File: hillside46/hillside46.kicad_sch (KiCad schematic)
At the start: 92 parts, among them J1 I2C, J2 TRRS, J3 Bat_Pos, J4 Bat_Neg, J5 FFC2B28-12-G, K1 SW_Key, K10 SW_Key, K11 SW_Key, K12 SW_Key, K13 SW_Key, K14 SW_Key, K15 SW_Key, K16 SW_Key, K17 SW_Key, K18 SW_Key, K19 SW_Rotary, K2 SW_Key, K20 SW_Rotary, K21 SW_Key, K22 SW_Key, K23 SW_Key, K3 SW_Key, K4 SW_Key, K5 SW_Key, K6 SW_Key, K7 SW_Key, K8 SW_Key, K9 SW_Key, SW1 SKQGAFE010, SW2 SW_Power, U1 NiceNano2_r, U2 SRV05-4

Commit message: Adding some JLCPCB part numbers
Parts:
- J5: JLC Type (none) -> Extended; LCSC (none) -> C271734; Price (none) -> 0.4155 @ 2+
- SW2: Config Optional -> (none); LCSC (none) -> C221662
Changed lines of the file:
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@@
       (effects (font (size 1.27 1.27)) hide)
     )
-    (property "LCSC" "" (id 4) (at 55.88 180.34 0)
+    (property "LCSC" "C221662" (id 4) (at 55.88 180.34 0)
       (effects (font (size 1.27 1.27)) hide)
     )
@@
       (effects (font (size 1.27 1.27)) hide)
     )
-    (property "Config" "Optional" (id 7) (at 55.88 180.34 0)
+    (property "Config" "" (id 7) (at 55.88 180.34 0)
       (effects (font (size 1.27 1.27)) hide)
     )
@@
       (effects (font (size 1.27 1.27)) (justify left bottom) hide)
     )
-    (pin "1")
+    (property "JLC Type" "Extended" (id 8) (at 243.84 146.05 0)
+      (effects (font (size 1.27 1.27)) hide)
+    )
+    (property "LCSC" "C271734" (id 9) (at 243.84 146.05 0)
+      (effects (font (size 1.27 1.27)) hide)
+    )
+    (property "Price" "0.4155 @ 2+" (id 10) (at 243.84 146.05 0)
+      (effects (font (size 1.27 1.27)) hide)
+    )
+    (pin "1")

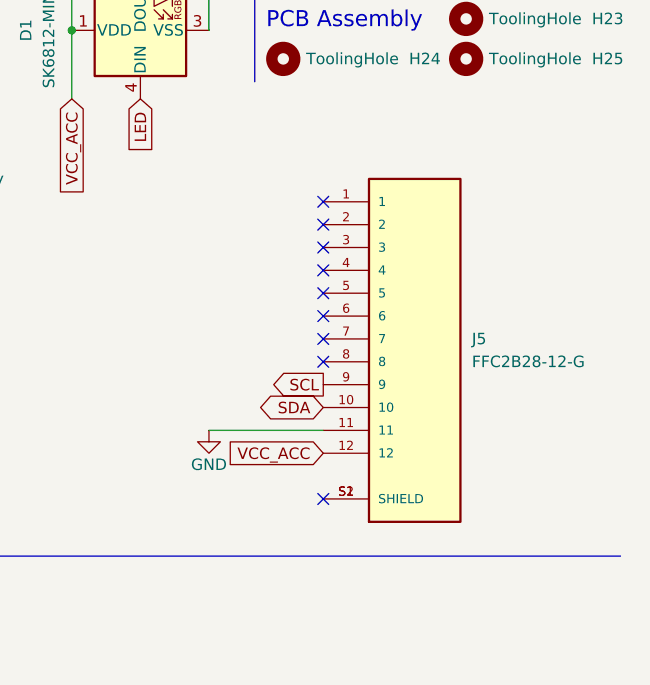
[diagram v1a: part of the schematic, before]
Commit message: Updating FFC connector to use the same footprint as JLCPCB part and rotating by 180 degrees to orient correctly
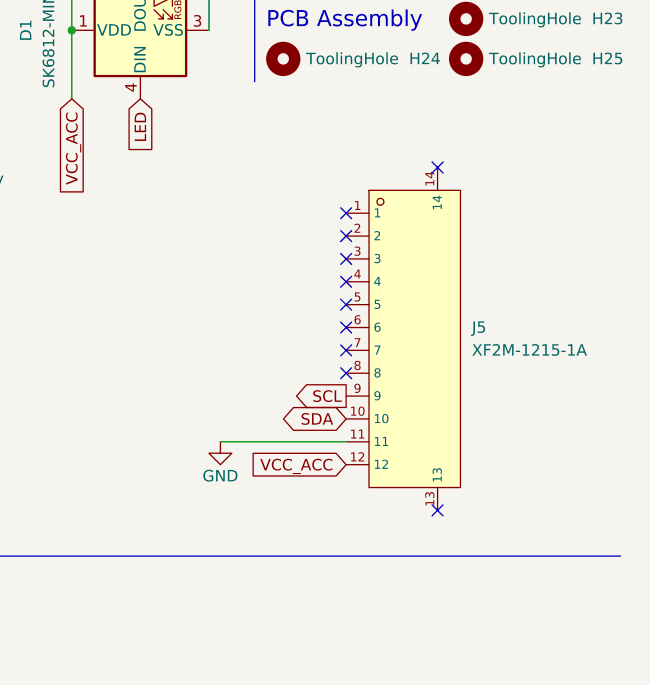
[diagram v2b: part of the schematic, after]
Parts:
- J5: value FFC2B28-12-G -> XF2M-1215-1A; footprint GCT_FFC2B28-12-G -> XF2M-1215-1A:FPC-SMD_12P-P0.50_XF2M-1215-1A; symbol FFC2B28-12-G:FFC2B28-12-G -> XF2M-1215-1A:XF2M-1215-1A
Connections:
- no-connect marks 14 -> 15
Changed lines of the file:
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@@
   (junction (at 176.53 142.24) (diameter 0) (color 0 0 0 0)
   )
-  (no_connect (at 233.68 163.83))
   (no_connect (at 213.36 50.8))
   (no_connect (at 102.87 154.94))
   (no_connect (at 135.255 184.15))
-  (no_connect (at 233.68 148.59))
-  (no_connect (at 233.68 143.51))
-  (no_connect (at 233.68 146.05))
-  (no_connect (at 233.68 138.43))
+  (no_connect (at 246.38 165.1))
+  (no_connect (at 236.22 134.62))
+  (no_connect (at 236.22 137.16))
+  (no_connect (at 236.22 139.7))
+  (no_connect (at 236.22 132.08))
+  (no_connect (at 236.22 149.86))
+  (no_connect (at 236.22 142.24))
+  (no_connect (at 236.22 144.78))
+  (no_connect (at 236.22 147.32))
+  (no_connect (at 246.38 127))
   (no_connect (at 99.06 154.94))
-  (no_connect (at 233.68 140.97))
-  (no_connect (at 233.68 130.81))
-  (no_connect (at 233.68 133.35))
-  (no_connect (at 233.68 135.89))
   (no_connect (at 60.96 177.8))
   (wire (pts (xy 172.72 57.15) (xy 180.975 57.15))
@@
     (stroke (width 0) (type default) (color 0 0 0 0))
   )
-  (wire (pts (xy 220.98 156.21) (xy 233.68 156.21))
-    (stroke (width 0) (type default) (color 0 0 0 0))
-  )
   (wire (pts (xy 14.605 36.195) (xy 14.605 50.165))
     (stroke (width 0) (type default) (color 0 0 0 0))
@@
     (stroke (width 0) (type default) (color 0 0 0 0))
   )
+  (wire (pts (xy 222.25 157.48) (xy 236.22 157.48))
+    (stroke (width 0) (type default) (color 0 0 0 0))
+  )
   (wire (pts (xy 220.98 93.98) (xy 220.98 76.2))
     (stroke (width 0) (type default) (color 0 0 0 0))
@@
     )
   )
-  (global_label "SCL" (shape output) (at 233.68 151.13 180) (fields_autoplaced)
+  (global_label "SCL" (shape output) (at 236.22 152.4 180) (fields_autoplaced)
     (effects (font (size 1.27 1.27)) (justify right))
-    (property "Intersheet References" "${INTERSHEET_REFS}" (id 0) (at 420.37 281.94 0)
+    (property "Intersheet References" "${INTERSHEET_REFS}" (id 0) (at 422.91 283.21 0)
       (effects (font (size 1.27 1.27)) hide)
     )
@@
     )
   )
-  (global_label "VCC_ACC" (shape input) (at 233.68 158.75 180) (fields_autoplaced)
+  (global_label "VCC_ACC" (shape input) (at 236.22 160.02 180) (fields_autoplaced)
     (effects (font (size 1.27 1.27)) (justify right))
-    (property "Intersheet References" "${INTERSHEET_REFS}" (id 0) (at 58.42 27.94 0)
+    (property "Intersheet References" "${INTERSHEET_REFS}" (id 0) (at 60.96 29.21 0)
       (effects (font (size 1.27 1.27)) hide)
     )
@@
     )
   )
-  (global_label "SDA" (shape bidirectional) (at 233.68 153.67 180) (fields_autoplaced)
+  (global_label "SDA" (shape bidirectional) (at 236.22 154.94 180) (fields_autoplaced)
     (effects (font (size 1.27 1.27)) (justify right))
-    (property "Intersheet References" "${INTERSHEET_REFS}" (id 0) (at 420.37 290.83 0)
+    (property "Intersheet References" "${INTERSHEET_REFS}" (id 0) (at 422.91 292.1 0)
       (effects (font (size 1.27 1.27)) hide)
     )
@@
     )
   )
-  (symbol (lib_id "power:GND") (at 220.98 156.21 0) (unit 1)
+  (symbol (lib_id "power:GND") (at 222.25 157.48 0) (unit 1)
     (in_bom yes) (on_board yes)
-    (property "Reference" "#PWR0105" (id 0) (at 220.98 162.56 0)
+    (property "Reference" "#PWR0105" (id 0) (at 222.25 163.83 0)
       (effects (font (size 1.27 1.27)) hide)
     )
-    (property "Value" "GND" (id 1) (at 220.98 160.02 0))
-    (property "Footprint" "" (id 2) (at 220.98 156.21 0)
+    (property "Value" "GND" (id 1) (at 222.25 161.29 0))
+    (property "Footprint" "" (id 2) (at 222.25 157.48 0)
       (effects (font (size 1.27 1.27)) hide)
     )
-    (property "Datasheet" "" (id 3) (at 220.98 156.21 0)
+    (property "Datasheet" "" (id 3) (at 222.25 157.48 0)
       (effects (font (size 1.27 1.27)) hide)
     )
@@
     )
   )
-  (symbol (lib_id "FFC2B28-12-G:FFC2B28-12-G") (at 243.84 146.05 0) (unit 1)
+  (symbol (lib_id "XF2M-1215-1A:XF2M-1215-1A") (at 243.84 132.08 0) (unit 1)
     (in_bom yes) (on_board yes) (fields_autoplaced)
-    (property "Reference" "J5" (id 0) (at 250.19 146.0499 0)
+    (property "Reference" "J5" (id 0) (at 250.19 144.7799 0)
       (effects (font (size 1.27 1.27)) (justify left))
     )
-    (property "Value" "FFC2B28-12-G" (id 1) (at 250.19 148.5899 0)
+    (property "Value" "XF2M-1215-1A" (id 1) (at 250.19 147.3199 0)
       (effects (font (size 1.27 1.27)) (justify left))
     )
-    (property "Footprint" "GCT_FFC2B28-12-G" (id 2) (at 243.84 146.05 0)
-      (effects (font (size 1.27 1.27)) (justify left bottom) hide)
+    (property "Footprint" "XF2M-1215-1A:FPC-SMD_12P-P0.50_XF2M-1215-1A" (id 2) (at 243.84 142.24 0)
+      (effects (font (size 1.27 1.27) italic) hide)
     )
-    (property "Datasheet" "" (id 3) (at 243.84 146.05 0)
-      (effects (font (size 1.27 1.27)) (justify left bottom) hide)
+    (property "Datasheet" "https://item.szlcsc.com/260768.html" (id 3) (at 241.554 131.953 0)
+      (effects (font (size 1.27 1.27)) (justify left) hide)
     )
-    (property "STANDARD" "Manufacturer Recommendations" (id 4) (at 243.84 146.05 0)
+    (property "STANDARD" "Manufacturer Recommendations" (id 4) (at 243.84 132.08 0)
       (effects (font (size 1.27 1.27)) (justify left bottom) hide)
     )
-    (property "MAXIMUM_PACKAGE_HEIGHT" "1.75mm" (id 5) (at 243.84 146.05 0)
+    (property "MAXIMUM_PACKAGE_HEIGHT" "1.75mm" (id 5) (at 243.84 132.08 0)
       (effects (font (size 1.27 1.27)) (justify left bottom) hide)
     )
-    (property "MANUFACTURER" "GCT" (id 6) (at 243.84 146.05 0)
+    (property "MANUFACTURER" "GCT" (id 6) (at 243.84 132.08 0)
       (effects (font (size 1.27 1.27)) (justify left bottom) hide)
     )
-    (property "PARTREV" "A" (id 7) (at 243.84 146.05 0)
+    (property "PARTREV" "A" (id 7) (at 243.84 132.08 0)
       (effects (font (size 1.27 1.27)) (justify left bottom) hide)
     )
-    (property "JLC Type" "Extended" (id 8) (at 243.84 146.05 0)
+    (property "JLC Type" "Extended" (id 8) (at 243.84 132.08 0)
       (effects (font (size 1.27 1.27)) hide)
     )
-    (property "LCSC" "C271734" (id 9) (at 243.84 146.05 0)
+    (property "LCSC" "C271734" (id 9) (at 243.84 132.08 0)
       (effects (font (size 1.27 1.27)) hide)
     )
-    (property "Price" "0.4155 @ 2+" (id 10) (at 243.84 146.05 0)
+    (property "Price" "0.4155 @ 2+" (id 10) (at 243.84 132.08 0)
       (effects (font (size 1.27 1.27)) hide)
     )
@@
     (pin "11")
     (pin "12")
+    (pin "13")
+    (pin "14")
     (pin "2")
     (pin "3")
@@
     (pin "8")
     (pin "9")
-    (pin "S1")
-    (pin "S2")
   )
   (symbol (lib_id "hillside_basic:Bumpon") (at 250.825 88.9 0) (unit 1)
@@
     )
     (path "/59b49660-470e-413c-8e82-343367586c1b"
-      (reference "J5") (unit 1) (value "FFC2B28-12-G") (footprint "GCT_FFC2B28-12-G")
+      (reference "J5") (unit 1) (value "XF2M-1215-1A") (footprint "XF2M-1215-1A:FPC-SMD_12P-P0.50_XF2M-1215-1A")
     )
     (path "/00000000-0000-0000-0000-000061a8564f"

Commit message: Updating pcb art
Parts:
- added G1: LOGO, wowee:wowee, symbol wowee:LOGO
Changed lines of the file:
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@@
     (pin "9")
+  )
+  (symbol (lib_id "wowee:LOGO") (at 149.86 146.05 0) (unit 1)
+    (in_bom yes) (on_board yes)
+    (property "Reference" "G1" (id 0) (at 149.86 138.43 0))
+    (property "Value" "LOGO" (id 1) (at 148.59 151.13 0))
+    (property "Footprint" "wowee:wowee" (id 2) (at 149.86 146.05 0)
+      (effects (font (size 1.27 1.27)) hide)
+    )
+    (property "Datasheet" "" (id 3) (at 149.86 146.05 0)
+      (effects (font (size 1.27 1.27)) hide)
+    )
   )
   (symbol (lib_id "hillside_basic:Bumpon") (at 250.825 88.9 0) (unit 1)
@@
       (reference "DS1") (unit 1) (value "Display") (footprint "hillside:NiceView")
     )
+    (path "/5bbedd43-59d1-4419-8a1b-47c04fffc312"
+      (reference "G1") (unit 1) (value "LOGO") (footprint "wowee:wowee")
+    )
     (path "/00000000-0000-0000-0000-00006147f195"

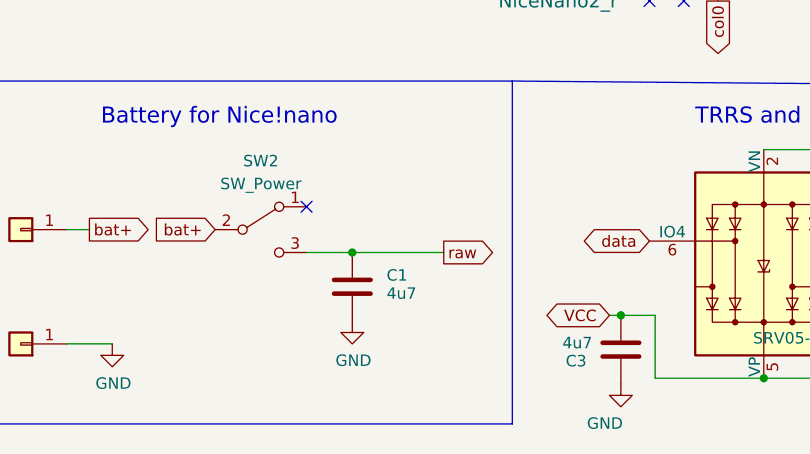
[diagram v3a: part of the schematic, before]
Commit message: Move switch, flip the copper on DS
Move the switch to the side of the PCB to make it easier to swtich.
Flip the copper layer for the display connector.
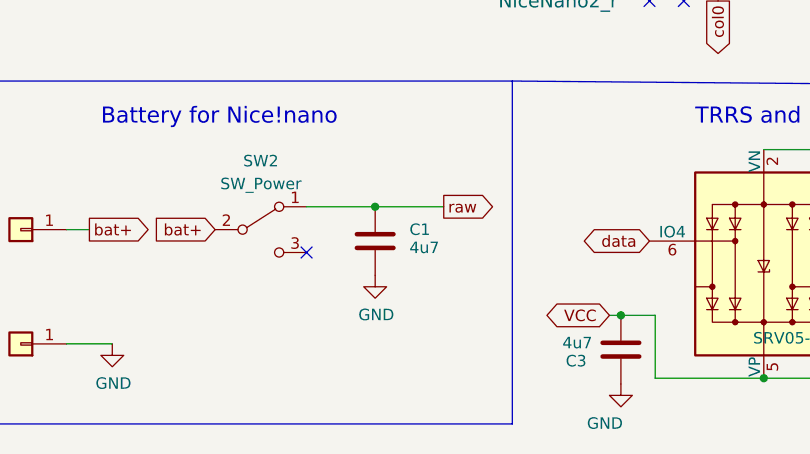
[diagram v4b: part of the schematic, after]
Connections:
- net raw: now also SW2.1 (A); no longer SW2.3 (C)
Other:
- moved on the sheet: C1
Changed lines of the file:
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@@
   (junction (at 205.74 76.2) (diameter 0) (color 0 0 0 0)
   )
-  (junction (at 66.04 182.88) (diameter 0) (color 0 0 0 0)
+  (junction (at 68.58 177.8) (diameter 0) (color 0 0 0 0)
   )
   (junction (at 186.055 86.995) (diameter 0) (color 0 0 0 0)
@@
   (no_connect (at 213.36 50.8))
   (no_connect (at 102.87 154.94))
+  (no_connect (at 60.96 182.88))
   (no_connect (at 135.255 184.15))
   (no_connect (at 246.38 165.1))
@@
   (no_connect (at 246.38 127))
   (no_connect (at 99.06 154.94))
-  (no_connect (at 60.96 177.8))
   (wire (pts (xy 172.72 57.15) (xy 180.975 57.15))
     (stroke (width 0) (type default) (color 0 0 0 0))
@@
     (stroke (width 0) (type default) (color 0 0 0 0))
   )
-  (wire (pts (xy 60.96 182.88) (xy 66.04 182.88))
+  (wire (pts (xy 60.96 177.8) (xy 68.58 177.8))
     (stroke (width 0) (type default) (color 0 0 0 0))
   )
@@
     (stroke (width 0) (type default) (color 0 0 0 0))
   )
-  (wire (pts (xy 66.04 182.88) (xy 76.2 182.88))
-    (stroke (width 0) (type default) (color 0 0 0 0))
-  )
   (wire (pts (xy 135.255 171.45) (xy 135.255 179.07))
     (stroke (width 0) (type default) (color 0 0 0 0))
@@
   )
   (wire (pts (xy 52.705 50.165) (xy 47.625 50.165))
+    (stroke (width 0) (type default) (color 0 0 0 0))
+  )
+  (wire (pts (xy 68.58 177.8) (xy 76.2 177.8))
     (stroke (width 0) (type default) (color 0 0 0 0))
   )
@@
     )
   )
-  (global_label "raw" (shape output) (at 76.2 182.88 0) (fields_autoplaced)
-    (effects (font (size 1.27 1.27)) (justify left))
-    (property "Intersheet References" "${INTERSHEET_REFS}" (id 0) (at -15.24 0 0)
-      (effects (font (size 1.27 1.27)) hide)
+  (global_label "raw" (shape output) (at 76.2 177.8 0) (fields_autoplaced)
+    (effects (font (size 1.27 1.27)) (justify left))
+    (property "Intersheet References" "${INTERSHEET_REFS}" (id 0) (at -15.24 -5.08 0)
+      (effects (font (size 1.27 1.27)) (justify right) hide)
     )
   )
@@
     (pin "1")
   )
-  (symbol (lib_id "power:GND") (at 66.04 190.5 0) (unit 1)
-    (in_bom yes) (on_board yes)
-    (property "Reference" "#PWR08" (id 0) (at 66.04 196.85 0)
-      (effects (font (size 1.27 1.27)) hide)
-    )
-    (property "Value" "GND" (id 1) (at 66.167 194.8942 0))
-    (property "Footprint" "" (id 2) (at 66.04 190.5 0)
-      (effects (font (size 1.27 1.27)) hide)
-    )
-    (property "Datasheet" "" (id 3) (at 66.04 190.5 0)
-      (effects (font (size 1.27 1.27)) hide)
-    )
-    (pin "1")
-  )
-  (symbol (lib_id "Device:C") (at 66.04 186.69 0) (unit 1)
-    (in_bom yes) (on_board yes)
-    (property "Reference" "C1" (id 0) (at 69.85 185.42 0)
+  (symbol (lib_id "power:GND") (at 68.58 185.42 0) (unit 1)
+    (in_bom yes) (on_board yes)
+    (property "Reference" "#PWR08" (id 0) (at 68.58 191.77 0)
+      (effects (font (size 1.27 1.27)) hide)
+    )
+    (property "Value" "GND" (id 1) (at 68.707 189.8142 0))
+    (property "Footprint" "" (id 2) (at 68.58 185.42 0)
+      (effects (font (size 1.27 1.27)) hide)
+    )
+    (property "Datasheet" "" (id 3) (at 68.58 185.42 0)
+      (effects (font (size 1.27 1.27)) hide)
+    )
+    (pin "1")
+  )
+  (symbol (lib_id "Device:C") (at 68.58 181.61 0) (unit 1)
+    (in_bom yes) (on_board yes)
+    (property "Reference" "C1" (id 0) (at 72.39 180.34 0)
       (effects (font (size 1.27 1.27)) (justify left))
     )
-    (property "Value" "4u7" (id 1) (at 69.85 186.69 0)
+    (property "Value" "4u7" (id 1) (at 72.39 181.61 0)
       (effects (font (size 1.27 1.27)) (justify left top))
     )
-    (property "Footprint" "hillside_basic:C_0805_2012Metric" (id 2) (at 67.0052 190.5 0)
-      (effects (font (size 1.27 1.27)) hide)
-    )
-    (property "Datasheet" "~" (id 3) (at 66.04 186.69 0)
-      (effects (font (size 1.27 1.27)) hide)
-    )
-    (property "JLC Type" "Basic" (id 4) (at 66.04 186.69 0)
-      (effects (font (size 1.27 1.27)) hide)
-    )
-    (property "LCSC" "C1779" (id 5) (at 66.04 186.69 0)
-      (effects (font (size 1.27 1.27)) hide)
-    )
-    (property "Price" ".01 @20+" (id 6) (at 66.04 186.69 0)
-      (effects (font (size 1.27 1.27)) hide)
-    )
+    (property "Footprint" "hillside_basic:C_0805_2012Metric" (id 2) (at 69.5452 185.42 0)
+      (effects (font (size 1.27 1.27)) hide)
+    )
+    (property "Datasheet" "~" (id 3) (at 68.58 181.61 0)
+      (effects (font (size 1.27 1.27)) hide)
+    )
+    (property "JLC Type" "Basic" (id 4) (at 68.58 181.61 0)
+      (effects (font (size 1.27 1.27)) hide)
+    )
+    (property "LCSC" "C1779" (id 5) (at 68.58 181.61 0)
+      (effects (font (size 1.27 1.27)) hide)
+    )
+    (property "Price" ".01 @20+" (id 6) (at 68.58 181.61 0)
+      (effects (font (size 1.27 1.27)) hide)
+    )

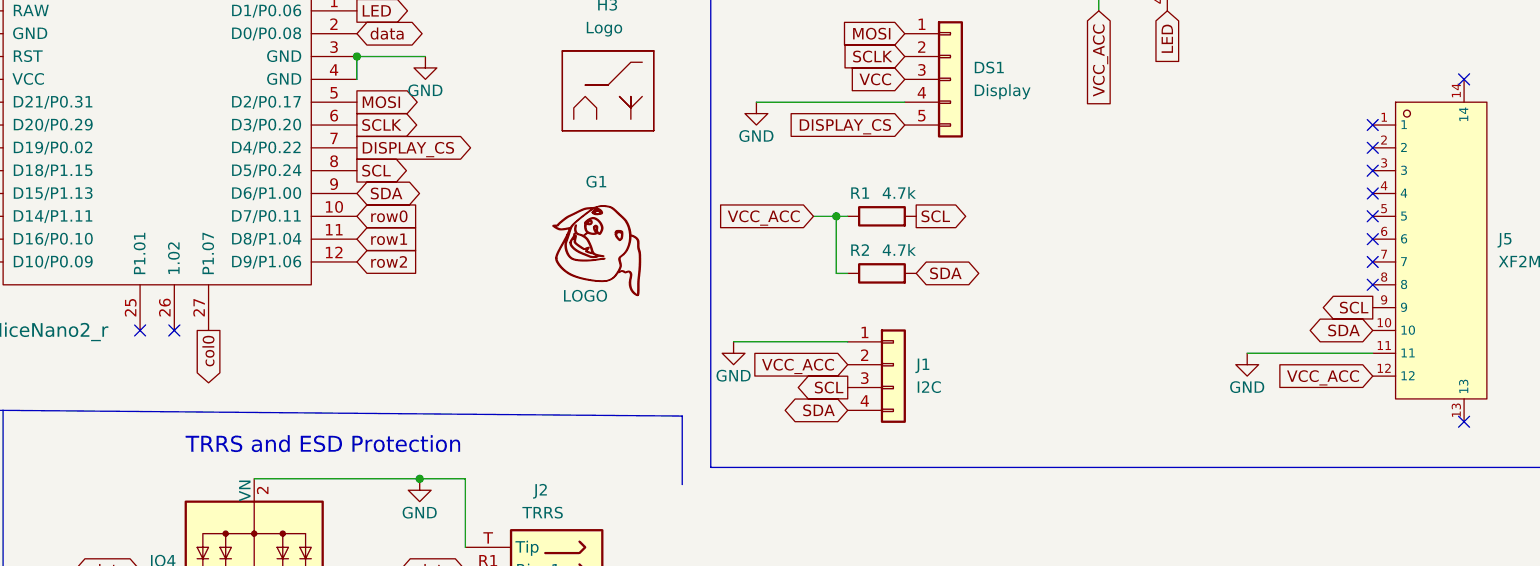
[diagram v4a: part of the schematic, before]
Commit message: Connecting the data ready pin
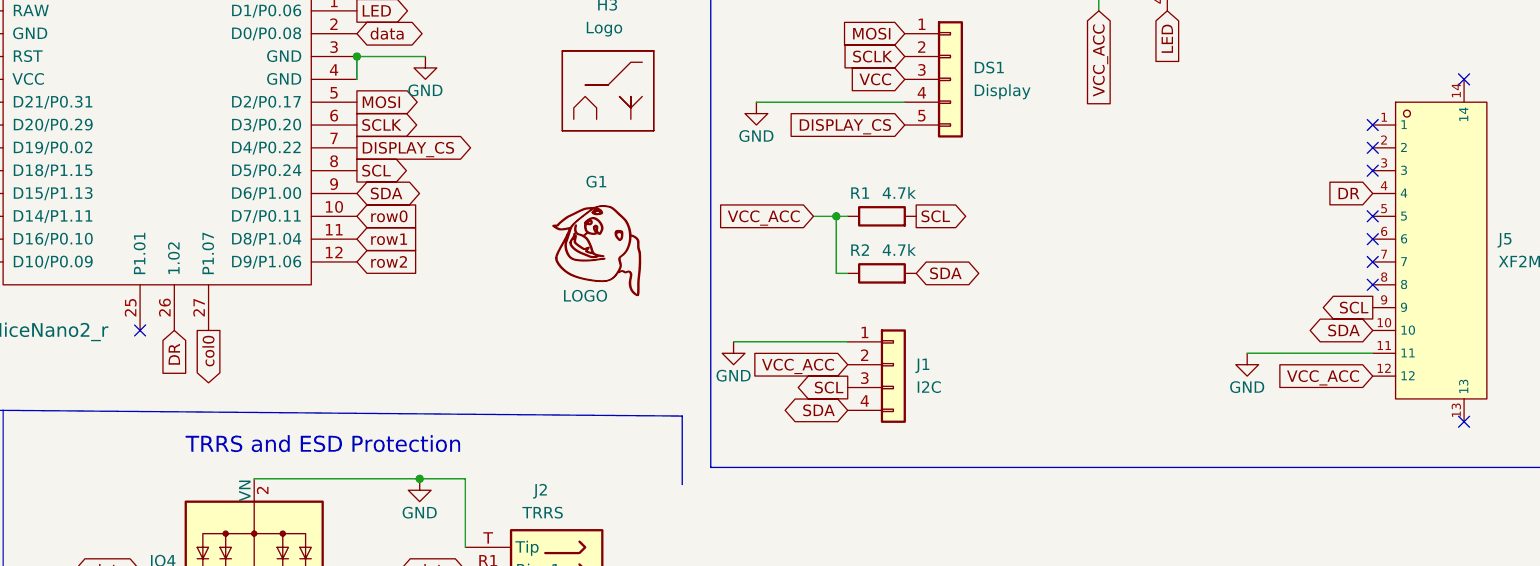
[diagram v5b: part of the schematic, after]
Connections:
- net DR: now reaches U1.26 (1.02)
- net DR: now also J5.4
- no-connect marks 15 -> 13
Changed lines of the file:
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@@
   )
   (no_connect (at 213.36 50.8))
-  (no_connect (at 102.87 154.94))
+  (no_connect (at 99.06 154.94))
   (no_connect (at 60.96 182.88))
   (no_connect (at 135.255 184.15))
@@
   (no_connect (at 236.22 134.62))
   (no_connect (at 236.22 137.16))
-  (no_connect (at 236.22 139.7))
   (no_connect (at 236.22 132.08))
   (no_connect (at 236.22 149.86))
@@
   (no_connect (at 236.22 147.32))
   (no_connect (at 246.38 127))
-  (no_connect (at 99.06 154.94))
   (wire (pts (xy 172.72 57.15) (xy 180.975 57.15))
     (stroke (width 0) (type default) (color 0 0 0 0))
@@
     )
   )
+  (global_label "DR" (shape input) (at 236.22 139.7 180) (fields_autoplaced)
+    (effects (font (size 1.27 1.27)) (justify right))
+    (property "Intersheet References" "${INTERSHEET_REFS}" (id 0) (at 231.3558 139.7794 0)
+      (effects (font (size 1.27 1.27)) (justify left) hide)
+    )
+  )
   (global_label "raw" (shape input) (at 78.74 119.38 180) (fields_autoplaced)
     (effects (font (size 1.27 1.27)) (justify right))
@@
     )
   )
+  (global_label "DR" (shape input) (at 102.87 154.94 270) (fields_autoplaced)
+    (effects (font (size 1.27 1.27)) (justify right))
+    (property "Intersheet References" "${INTERSHEET_REFS}" (id 0) (at 102.9494 159.8042 90)
+      (effects (font (size 1.27 1.27)) (justify left) hide)
+    )
+  )
